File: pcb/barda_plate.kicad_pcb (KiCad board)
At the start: 2 copper layers, 228.6 x 76.2 mm, 44 parts, among them SW2 KEY_SWITCH

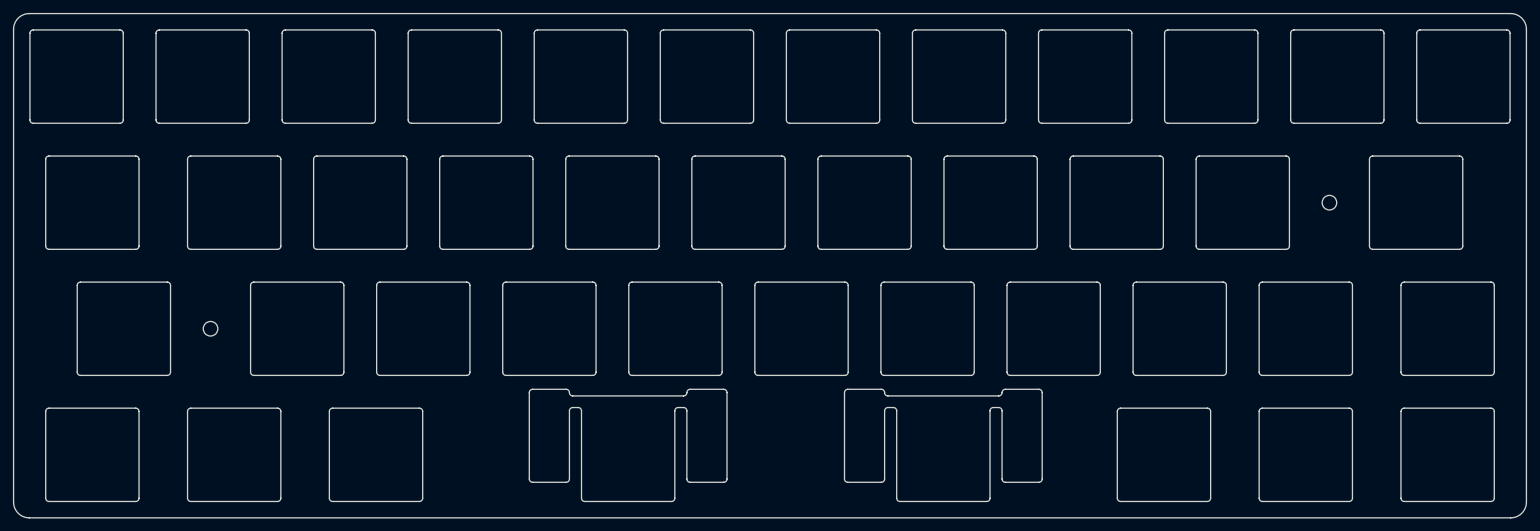
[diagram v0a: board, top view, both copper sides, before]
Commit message: Add case 3D models and update PCB assets
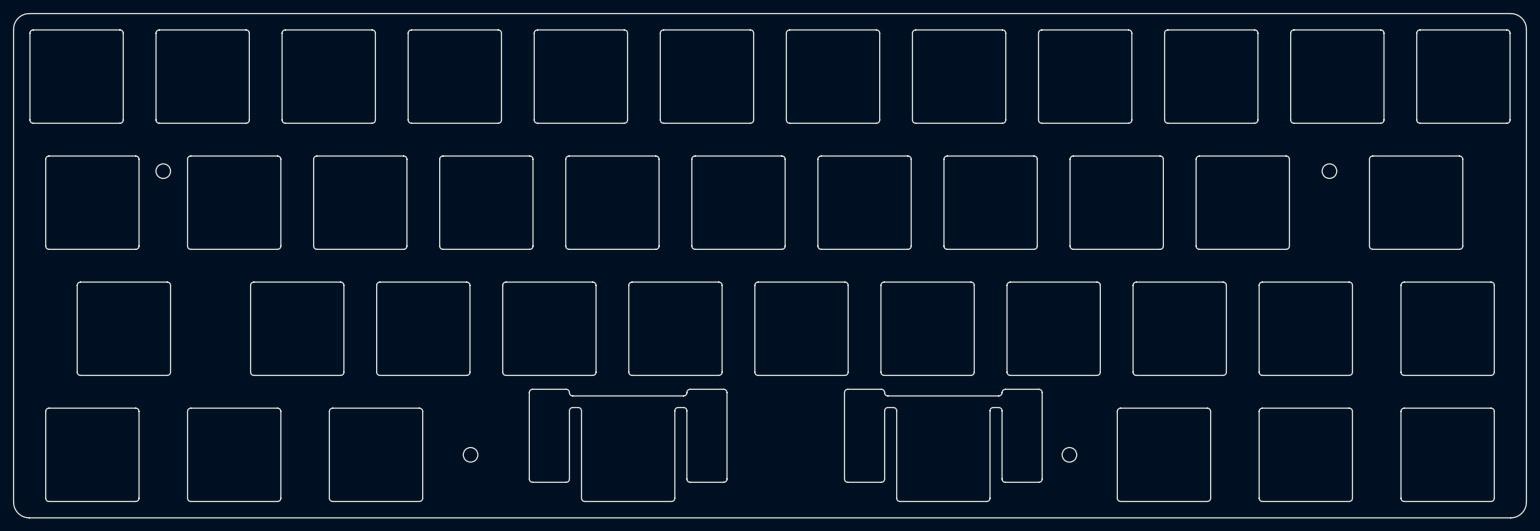
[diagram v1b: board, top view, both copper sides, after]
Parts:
- added REF**: MountingHole_2.2mm_M2, MountingHole:MountingHole_2.2mm_M2, F.Cu at (169.1, 85.7)
- added REF**: MountingHole_2.2mm_M2, MountingHole:MountingHole_2.2mm_M2, F.Cu at (32.1, 42.9)
- moved REF** 43.7 mm to (78.6, 85.7)
- moved REF** 4.76 mm to (208.4, 42.9)
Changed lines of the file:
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@@
 	(generator_version "10.0")
 	(general
-		(thickness 1.6)
+		(thickness 1.29)
 		(legacy_teardrops no)
 	)
@@
 	)
 	(setup
+		(stackup
+			(layer "F.SilkS"
+				(type "Top Silk Screen")
+			)
+			(layer "F.Paste"
+				(type "Top Solder Paste")
+			)
+			(layer "F.Mask"
+				(type "Top Solder Mask")
+				(thickness 0.01)
+			)
+			(layer "F.Cu"
+				(type "copper")
+				(thickness 0.035)
+			)
+			(layer "dielectric 1"
+				(type "core")
+				(thickness 1.2)
+				(material "FR4")
+				(epsilon_r 4.5)
+				(loss_tangent 0.02)
+			)
+			(layer "B.Cu"
+				(type "copper")
+				(thickness 0.035)
+			)
+			(layer "B.Mask"
+				(type "Bottom Solder Mask")
+				(thickness 0.01)
+			)
+			(layer "B.Paste"
+				(type "Bottom Solder Paste")
+			)
+			(layer "B.SilkS"
+				(type "Bottom Silk Screen")
+			)
+			(copper_finish "None")
+			(dielectric_constraints no)
+		)
 		(pad_to_mask_clearance 0)
 		(allow_soldermask_bridges_in_footprints no)
@@
 		(embedded_fonts no)
 	)
+	(footprint "MountingHole:MountingHole_2.2mm_M2"
+		(layer "F.Cu")
+		(at 169.06875 85.725)
+		(descr "Mounting Hole 2.2mm, M2, no annular, generated by kicad-footprint-generator mountinghole.py")
+		(tags "mountinghole M2")
+		(property "Reference" "REF**"
+			(at 0 -3.15 0)
+			(layer "F.SilkS")
+			(hide yes)
+			(effects
+				(font
+					(size 1 1)
+					(thickness 0.15)
+				)
+			)
+		)
+		(property "Value" "MountingHole_2.2mm_M2"
+			(at 0 3.15 0)
+			(layer "F.Fab")
+			(effects
+				(font
+					(size 1 1)
+					(thickness 0.15)
+				)
+			)
+		)
+		(property "Datasheet" ""
+			(at 0 0 0)
+			(layer "F.Fab")
+			(hide yes)
+			(effects
+				(font
+					(size 1.27 1.27)
+				)
+			)
+		)
+		(property "Description" ""
+			(at 0 0 0)
+			(layer "F.Fab")
+			(hide yes)
+			(effects
+				(font
+					(size 1.27 1.27)
+				)
+			)
+		)
+		(property "KiLib_Generator" "mounting_hardware/mounting_hole"
+			(at 0 0 0)
+			(layer "F.SilkS")
+			(hide yes)
+			(effects
+				(font
+					(size 1 1)
+					(thickness 0.15)
+				)
+			)
+		)
+		(attr exclude_from_pos_files exclude_from_bom)
+		(duplicate_pad_numbers_are_jumpers no)
+		(fp_circle
+			(center 0 0)
+			(end 2.2 0)
+			(stroke
+				(width 0.15)
+				(type solid)
+			)
+			(fill no)
+			(layer "Cmts.User")
+		)
+		(fp_circle
+			(center 0 0)
+			(end 2.45 0)
+			(stroke
+				(width 0.05)
+				(type solid)
+			)
+			(fill no)
+			(layer "F.CrtYd")
+		)
+		(fp_text user "${REFERENCE}"
+			(at 0 0 0)
+			(layer "F.Fab")
+			(effects
+				(font
+					(size 1 1)
+					(thickness 0.15)
+				)
+			)
+		)
+		(pad "" np_thru_hole circle
+			(at 0 0)
+			(size 2.2 2.2)
+			(drill 2.2)
+			(layers "*.Cu" "*.Mask")
+		)
+		(embedded_fonts no)
+	)
 	(footprint "Smidr:Plate_Smidr_Key_Hole"
 		(layer "F.Cu")
@@
 	(footprint "MountingHole:MountingHole_2.2mm_M2"
 		(layer "F.Cu")
-		(at 39.290625 66.675)
+		(at 78.58125 85.725)
 		(descr "Mounting Hole 2.2mm, M2, no annular, generated by kicad-footprint-generator mountinghole.py")
 		(tags "mountinghole M2")
@@
 	(footprint "MountingHole:MountingHole_2.2mm_M2"
 		(layer "F.Cu")
-		(at 208.359375 47.625)
+		(at 208.359375 42.8625)
 		(descr "Mounting Hole 2.2mm, M2, no annular, generated by kicad-footprint-generator mountinghole.py")
 		(tags "mountinghole M2")
@@
 		)
 		(embedded_fonts no)
+	)
+	(footprint "MountingHole:MountingHole_2.2mm_M2"
+		(layer "F.Cu")
+		(at 32.146875 42.8625)
+		(descr "Mounting Hole 2.2mm, M2, no annular, generated by kicad-footprint-generator mountinghole.py")
+		(tags "mountinghole M2")
+		(property "Reference" "REF**"
+			(at 0 -3.15 0)
+			(layer "F.SilkS")
+			(hide yes)
+			(effects
+				(font
+					(size 1 1)
+					(thickness 0.15)
+				)
+			)
+		)
+		(property "Value" "MountingHole_2.2mm_M2"
+			(at 0 3.15 0)
+			(layer "F.Fab")
+			(effects
+				(font
+					(size 1 1)
+					(thickness 0.15)
+				)
+			)
+		)
+		(property "Datasheet" ""
+			(at 0 0 0)
+			(layer "F.Fab")
+			(hide yes)
+			(effects
+				(font
+					(size 1.27 1.27)
+				)
+			)
+		)
+		(property "Description" ""
+			(at 0 0 0)
+			(layer "F.Fab")
+			(hide yes)
+			(effects
+				(font
+					(size 1.27 1.27)
+				)
+			)
+		)
+		(property "KiLib_Generator" "mounting_hardware/mounting_hole"
+			(at 0 0 0)
+			(layer "F.SilkS")
+			(hide yes)
+			(effects
+				(font
+					(size 1 1)
+					(thickness 0.15)
+				)
+			)
+		)
+		(attr exclude_from_pos_files exclude_from_bom)
+		(duplicate_pad_numbers_are_jumpers no)
+		(fp_circle
+			(center 0 0)
+			(end 2.2 0)
+			(stroke
+				(width 0.15)
+				(type solid)
+			)
+			(fill no)
+			(layer "Cmts.User")
+		)
+		(fp_circle
+			(center 0 0)
+			(end 2.45 0)
+			(stroke
+				(width 0.05)
+				(type solid)
+			)
+			(fill no)
+			(layer "F.CrtYd")
+		)
+		(fp_text user "${REFERENCE}"
+			(at 0 0 0)
+			(layer "F.Fab")
+			(effects
+				(font
+					(size 1 1)
+					(thickness 0.15)
+				)
+			)
+		)
+		(pad "" np_thru_hole circle
+			(at 0 0)
+			(size 2.2 2.2)
+			(drill 2.2)
+			(layers "*.Cu" "*.Mask")
+		)
+		(embedded_fonts no)

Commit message: Remove unused footprints
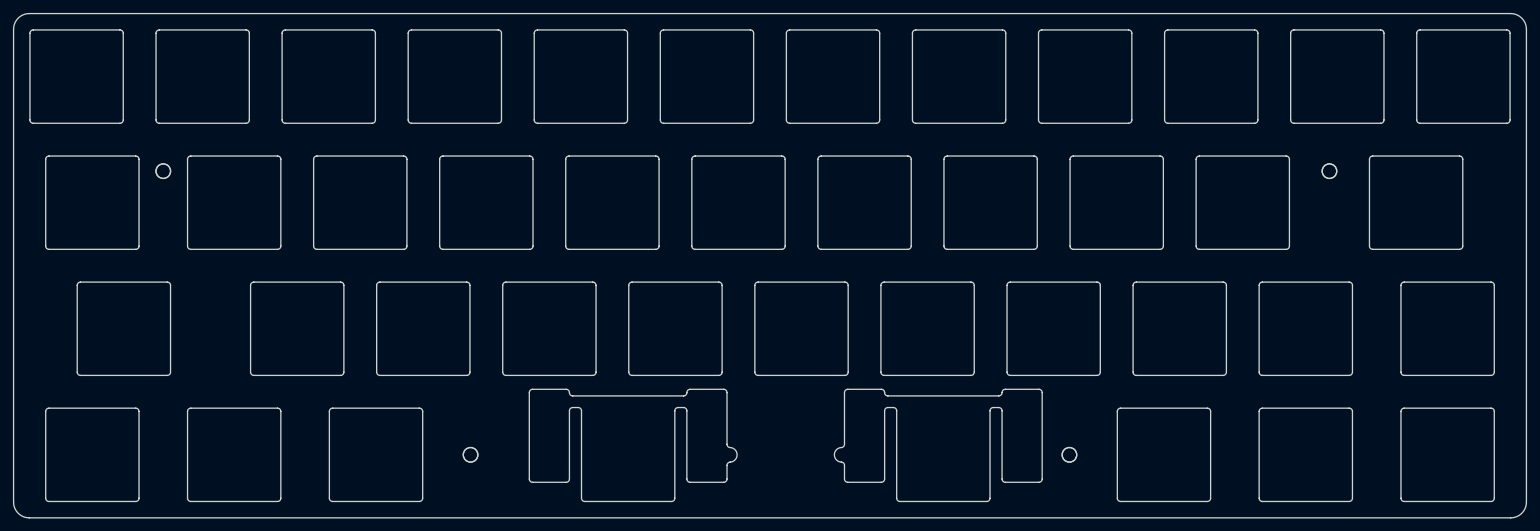
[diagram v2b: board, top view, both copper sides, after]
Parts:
- removed PH1: Tab, Smidr:Plate_Smidr_Key_Hole
- removed PH10: O, Smidr:Plate_Smidr_Key_Hole
- removed PH11: P, Smidr:Plate_Smidr_Key_Hole
- removed PH12: [, Smidr:Plate_Smidr_Key_Hole
- removed PH13, PH41: Caps, Smidr:Plate_Smidr_Key_Hole
- removed PH14: A, Smidr:Plate_Smidr_Key_Hole
- removed PH15: S, Smidr:Plate_Smidr_Key_Hole
- removed PH16: D, Smidr:Plate_Smidr_Key_Hole
- removed PH17: F, Smidr:Plate_Smidr_Key_Hole
- removed PH18: G, Smidr:Plate_Smidr_Key_Hole
- removed PH19: H, Smidr:Plate_Smidr_Key_Hole
- removed PH2: Q, Smidr:Plate_Smidr_Key_Hole
- removed PH20: J, Smidr:Plate_Smidr_Key_Hole
- removed PH21: K, Smidr:Plate_Smidr_Key_Hole
- removed PH22: L, Smidr:Plate_Smidr_Key_Hole
- removed PH23: ;, Smidr:Plate_Smidr_Key_Hole
- removed PH24: Z, Smidr:Plate_Smidr_Key_Hole
- removed PH25: X, Smidr:Plate_Smidr_Key_Hole
- removed PH26: C, Smidr:Plate_Smidr_Key_Hole
- removed PH27: V, Smidr:Plate_Smidr_Key_Hole
- removed PH28: B, Smidr:Plate_Smidr_Key_Hole
- removed PH29: N, Smidr:Plate_Smidr_Key_Hole
- removed PH3: W, Smidr:Plate_Smidr_Key_Hole
- removed PH30: M, Smidr:Plate_Smidr_Key_Hole
- removed PH31: ,, Smidr:Plate_Smidr_Key_Hole
- removed PH32: ., Smidr:Plate_Smidr_Key_Hole
- removed PH33: /, Smidr:Plate_Smidr_Key_Hole
- removed PH34: Ctrl, Smidr:Plate_Smidr_Key_Hole
- removed PH35, PH39: Win, Smidr:Plate_Smidr_Key_Hole
- removed PH36, PH38: Alt, Smidr:Plate_Smidr_Key_Hole
- removed PH4: E, Smidr:Plate_Smidr_Key_Hole
- removed PH40: Menu, Smidr:Plate_Smidr_Key_Hole
- removed PH5: R, Smidr:Plate_Smidr_Key_Hole
- removed PH6: T, Smidr:Plate_Smidr_Key_Hole
- removed PH7: Y, Smidr:Plate_Smidr_Key_Hole
- removed PH8: U, Smidr:Plate_Smidr_Key_Hole
- removed PH9: I, Smidr:Plate_Smidr_Key_Hole
- removed SW2: KEY_SWITCH, Smidr:Stab_Hole_Choc_v2_PlateMount_2.25u
- removed SW2: KEY_SWITCH, Smidr:Stab_Hole_Choc_v2_PlateMount_2u
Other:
- outline, holes or cut-outs redrawn

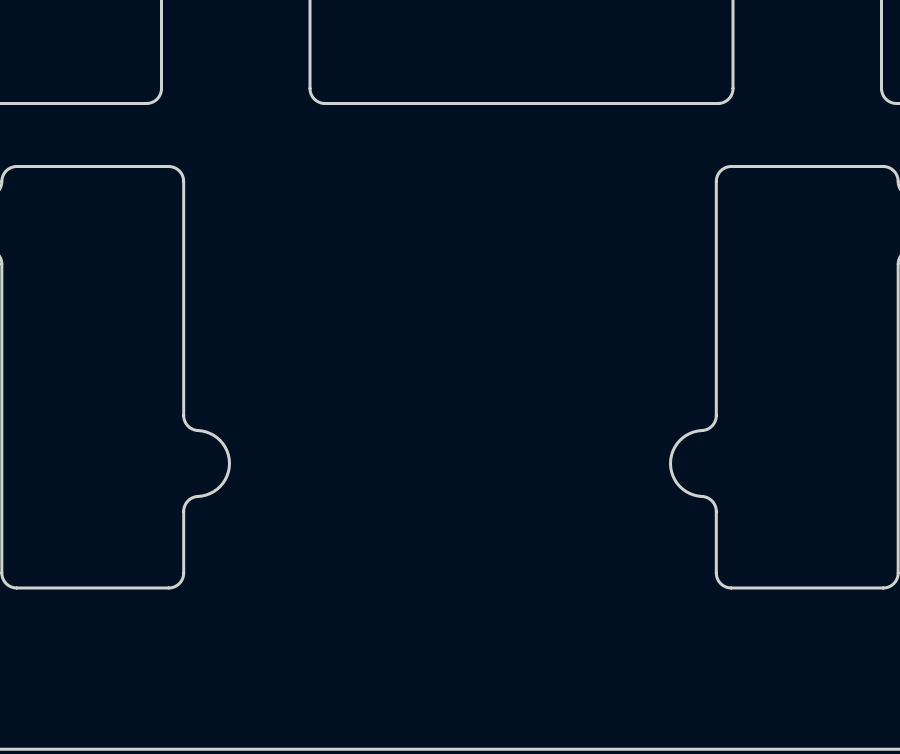
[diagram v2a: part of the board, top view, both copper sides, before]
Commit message: Update PCB and case for M2 4mm standoffs
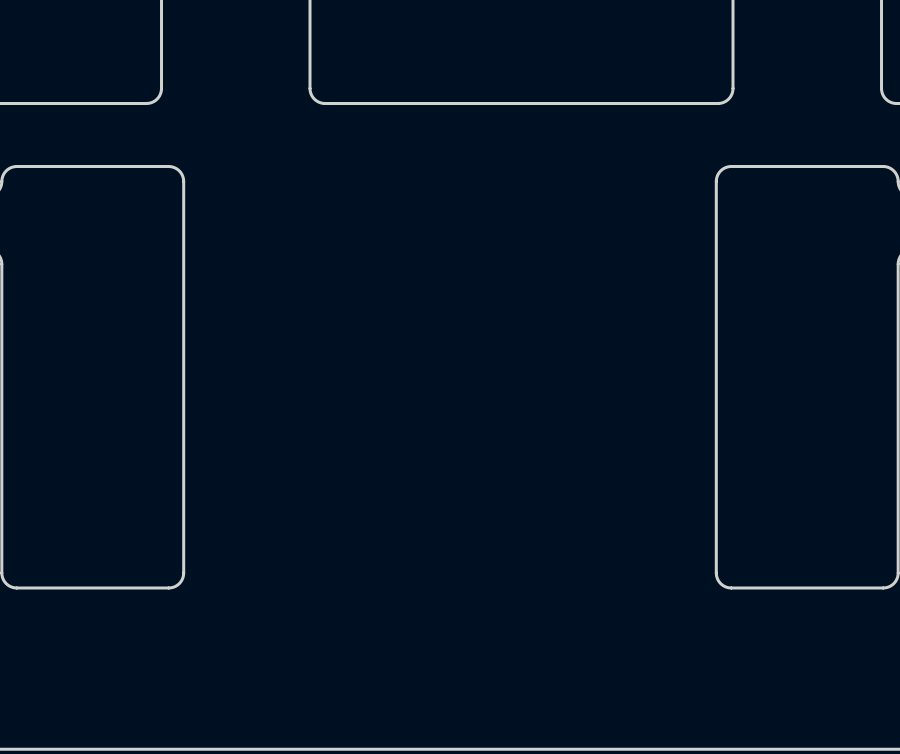
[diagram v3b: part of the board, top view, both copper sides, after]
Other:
- outline, holes or cut-outs redrawn
